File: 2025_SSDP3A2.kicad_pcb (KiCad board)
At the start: 4 copper layers, 58.4 x 28.8 mm, 62 parts, among them J1 SolderPad, J2 SolderPad, J3 SolderPad, J4 SolderPad, Q1 CSD19534Q5A, Q2 BSC0805LS, U1 LM5146RGYR

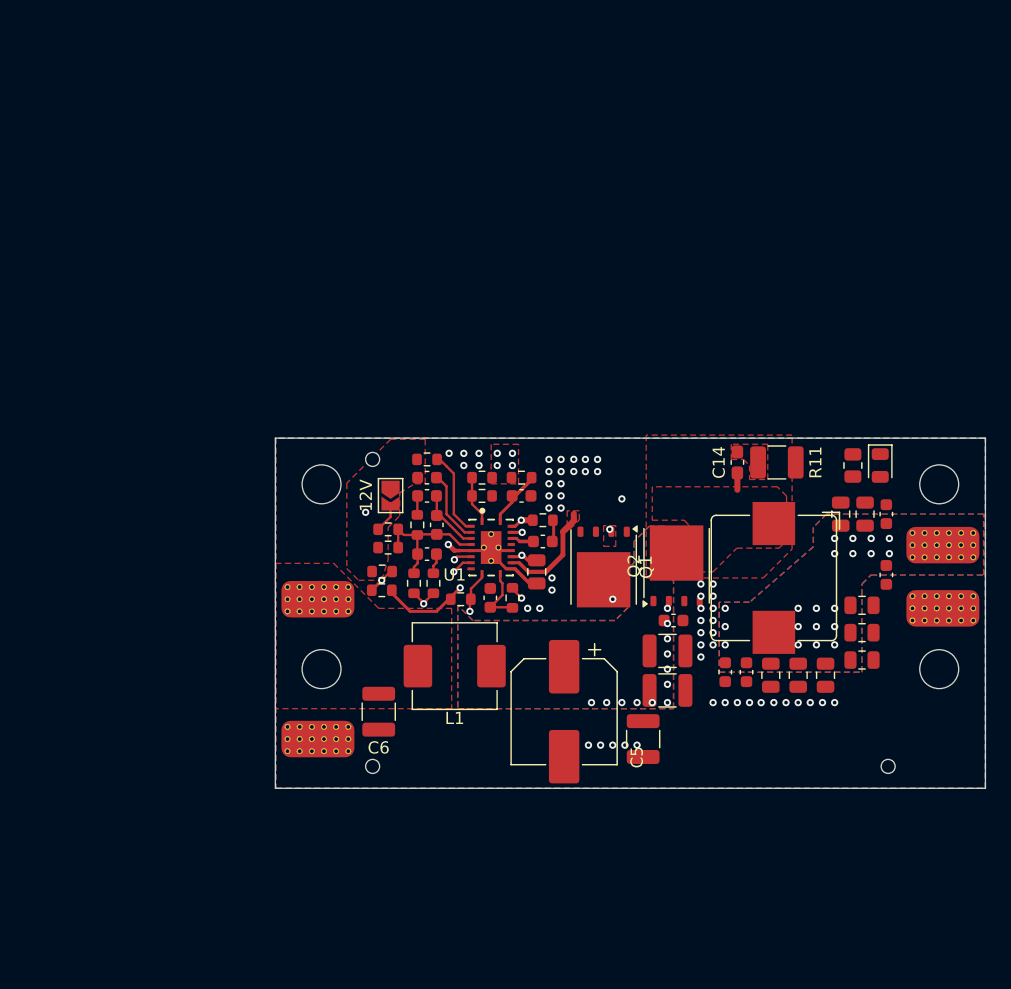
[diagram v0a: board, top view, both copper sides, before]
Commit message: Revised PCB layout
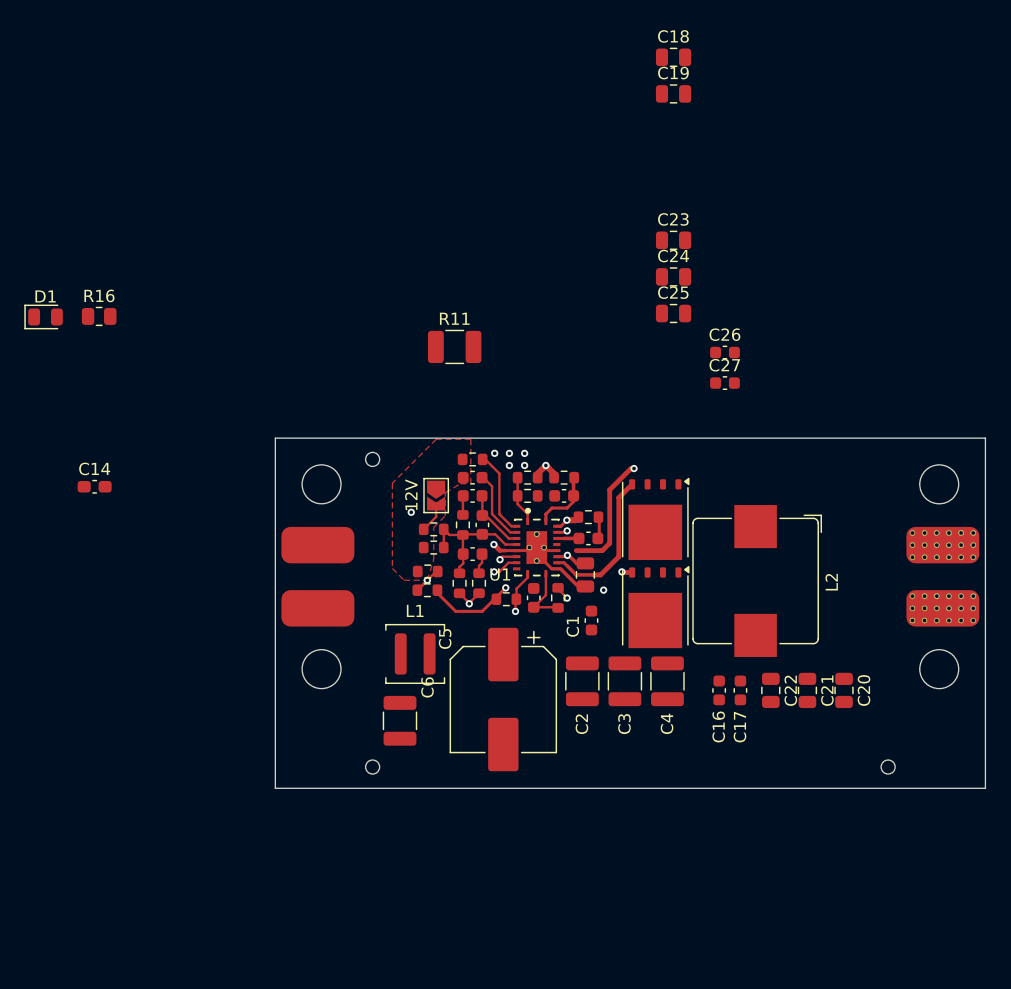
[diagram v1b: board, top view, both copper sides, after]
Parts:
- L1: footprint Inductor_SMD:L_Changjiang_FXL0630 -> Inductor_SMD:L_Coilcraft_XAL4040-XXX
- moved D1 69.7 mm to (101.1, 90.0), turned to 0 degrees
- moved R16 63.2 mm to (105.5, 90.0), turned to 0 degrees
- moved C14 52.9 mm to (105.1, 104.0), turned to 0 degrees
- moved C18 51.4 mm to (152.8, 68.7), turned to 0 degrees
- moved C19 48.9 mm to (152.8, 71.7), turned to 0 degrees
- moved C23 33.8 mm to (152.8, 83.7)
- moved R11 28.2 mm to (134.8, 92.5)
- moved C24 23.9 mm to (152.8, 86.7), turned to 0 degrees
- moved C25 22.8 mm to (152.8, 89.8), turned to 0 degrees
- moved C27 20.6 mm to (157.0, 95.5), turned to 0 degrees
- moved C26 18.8 mm to (157.0, 93.0), turned to 0 degrees
- moved J2 10.8 mm to (123.5, 114.0), turned to 90 degrees
- moved C22 8.88 mm to (160.8, 120.8), turned to -90 degrees
- moved C2 7.43 mm to (145.2, 120.0), turned to -90 degrees
- moved C1 6.75 mm to (146.0, 115.0), turned to 90 degrees
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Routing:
- net /SW: track 21.2 -> 3.47 mm, vias 5 -> 2
- net PGND: track 5.67 -> 16.2 mm, vias 51 -> 7
- net /LO: track 8.91 -> 12.5 mm, vias 2 -> 0
- net VIN: track 0.00 -> 2.56 mm, vias 16 -> 1
- net /U1_VIN: track 4.66 -> 5.29 mm
- net /HO: track 8.23 -> 7.62 mm
- net VOUT: vias 21 -> 1
- removed copper zone on F.Cu, net /HO
- removed copper zone on F.Cu, net /LO
- removed copper zone on F.Cu, net /SNUB_RC
- removed copper zone on F.Cu, net /SW
- removed copper zone on B.Cu, net PGND
- removed copper zone on F.Cu, net PGND
- removed copper zone on In1.Cu, net PGND
- removed copper zone on In2.Cu, net PGND
- removed copper zone on F.Cu, net VBAT
- removed copper zone on B.Cu, net VIN
- removed copper zone on F.Cu, net VIN
- removed copper zone on B.Cu, net VOUT
- removed copper zone on F.Cu, net VOUT

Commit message: Revised PCB layout
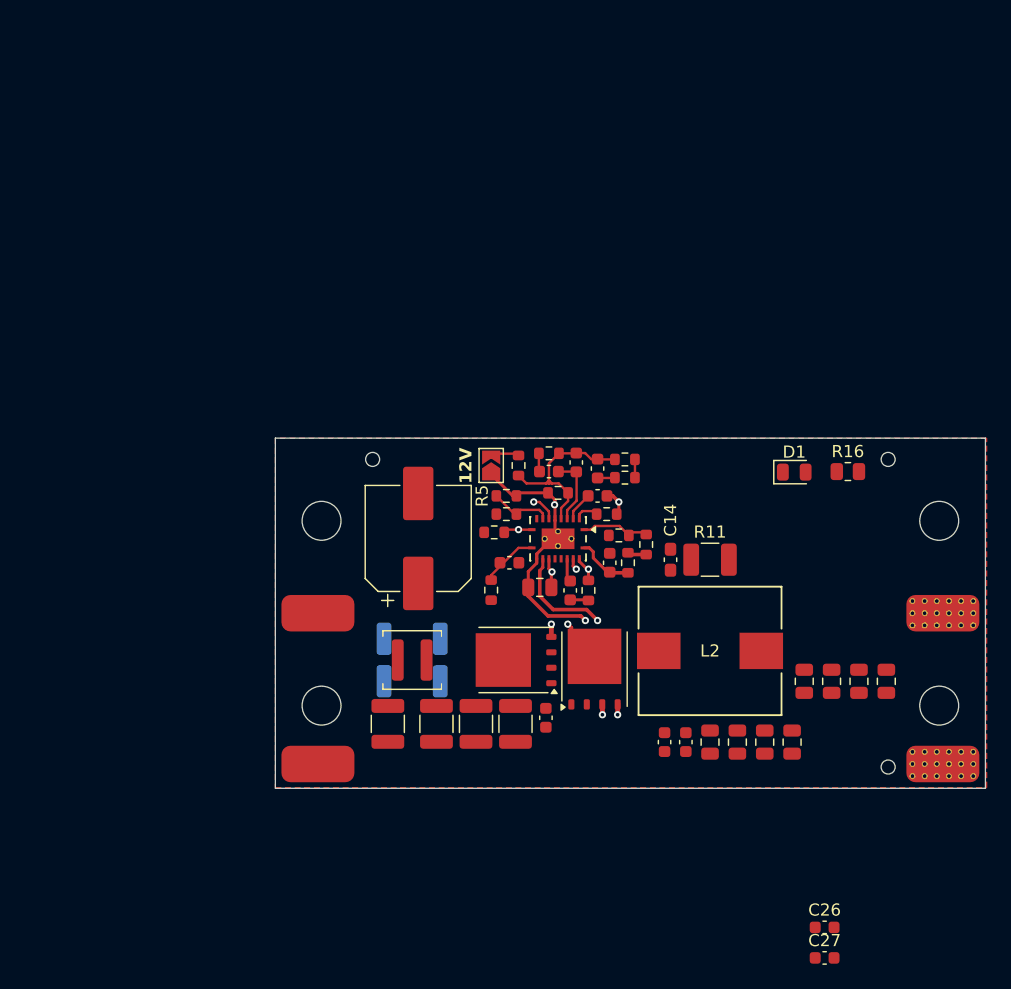
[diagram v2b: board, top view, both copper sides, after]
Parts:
- added R17: 0, Resistor_SMD:R_2010_5025Metric, B.Cu at (131.2, 116.5)
- added R18: 0, Resistor_SMD:R_2010_5025Metric, B.Cu at (131.2, 120.0)
- L2: footprint Inductor_SMD:L_Bourns_SRP1038C_10.0x10.0mm -> PA4342-472NLT:IND_PA4342_PUL-M
- Q2: value BSC0805LS -> BSC098N10NS5
- R1: value 24k -> 27k
- R3: value 9.1k -> 12k
- moved D1 62.9 mm to (162.7, 102.8)
- moved R16 62.9 mm to (167.1, 102.8)
- moved C18 56.4 mm to (155.8, 125.0), turned to -90 degrees
- moved C19 53.6 mm to (158.0, 125.0), turned to -90 degrees
- moved H5 49.4 mm to (170.4, 101.8)
- moved C26 48.0 mm to (165.2, 140.2)
- moved C27 48.0 mm to (165.2, 142.8)
- moved C14 47.7 mm to (152.5, 110.0), turned to 90 degrees
- moved C23 38.5 mm to (165.8, 120.0), turned to -90 degrees
- moved C24 36.6 mm to (168.0, 120.0), turned to -90 degrees
- moved C25 34.9 mm to (170.2, 120.0), turned to -90 degrees
- moved R11 27.3 mm to (155.8, 110.0)
- moved R14 17.0 mm to (148.8, 101.8), turned to 180 degrees
- moved C5 15.0 mm to (131.8, 108.2), turned to 90 degrees
- moved R12 14.8 mm to (148.8, 103.2), turned to 180 degrees
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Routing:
- net VCC: track 16.4 -> 2.47 mm, vias 2 -> 1
- net /SW: track 3.47 -> 10.7 mm
- net AGND: track 9.95 -> 15.5 mm
- net /LO: track 12.5 -> 17.9 mm, vias 0 -> 2
- net SYNCIN: track 10.2 -> 4.99 mm, vias 2 -> 0
- net /RT: track 7.10 -> 2.01 mm
- net PGND: track 16.2 -> 20.9 mm, vias 7 -> 2
- net /SS_TRK: track 6.39 -> 2.38 mm
- net /FB: track 11.6 -> 15.4 mm
- net /U1_EN: track 3.94 -> 5.58 mm
- net PG: track 3.48 -> 2.37 mm
- net VIN: track 2.56 -> 1.56 mm, vias 1 -> 0
- net /U1_VIN: track 5.29 -> 4.39 mm
- net VOUT: track 2.39 -> 1.50 mm, vias 1 -> 0
- net /ILIM: track 5.40 -> 4.68 mm
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- added copper zone on F.Cu, net PGND
- removed copper zone on F.Cu, net AGND
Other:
- board text added: "12V"

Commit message: Revised ILIM setting, added TVS
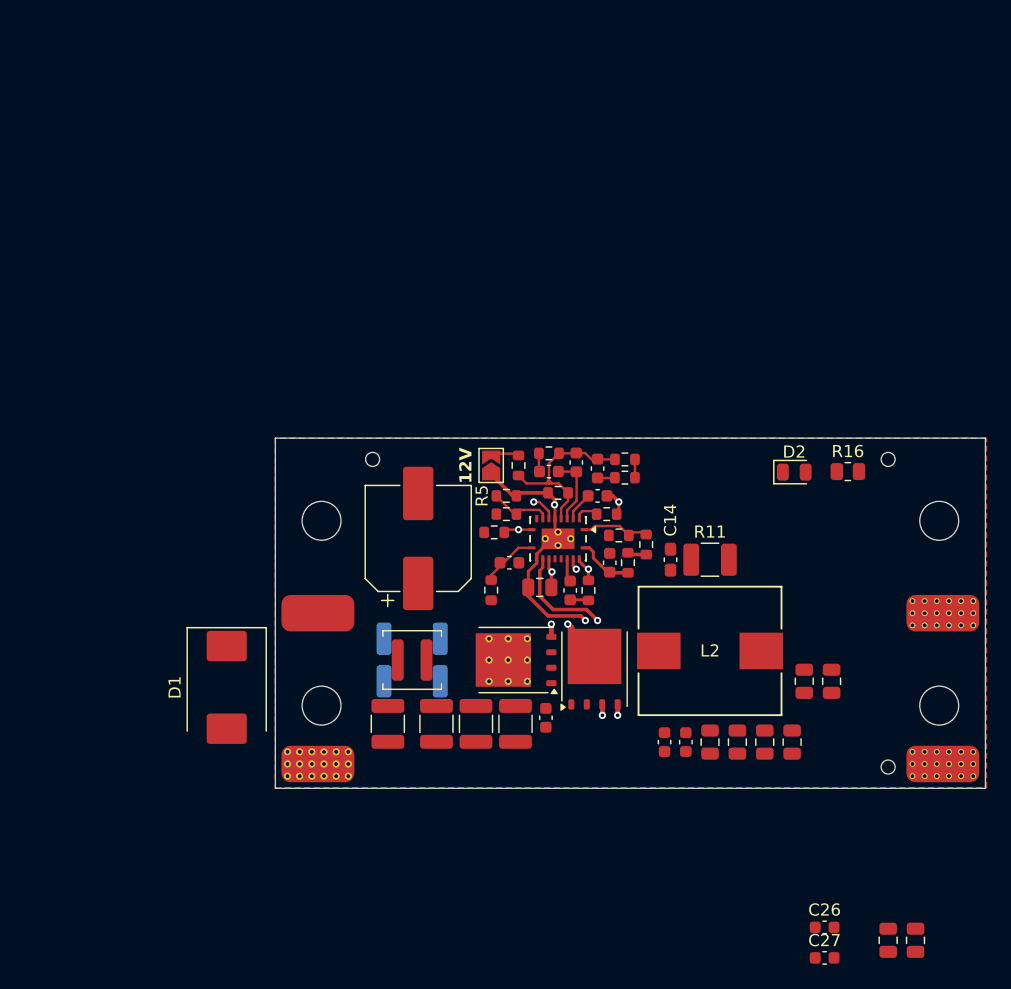
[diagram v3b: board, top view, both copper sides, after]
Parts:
- added D1: 70V, Diode_SMD:D_SMC, F.Cu at (116.0, 120.5)
- C11: value 10pF -> 22pF
- Q2: value BSC098N10NS5 -> BSC0805LS
- R8: value 470 -> 270
- moved C24 21.4 mm to (170.4, 141.3)
- moved C25 21.4 mm to (172.7, 141.3)
- renumbered D1 to D2

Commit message: Revised PCB layout, simplified EMI filter
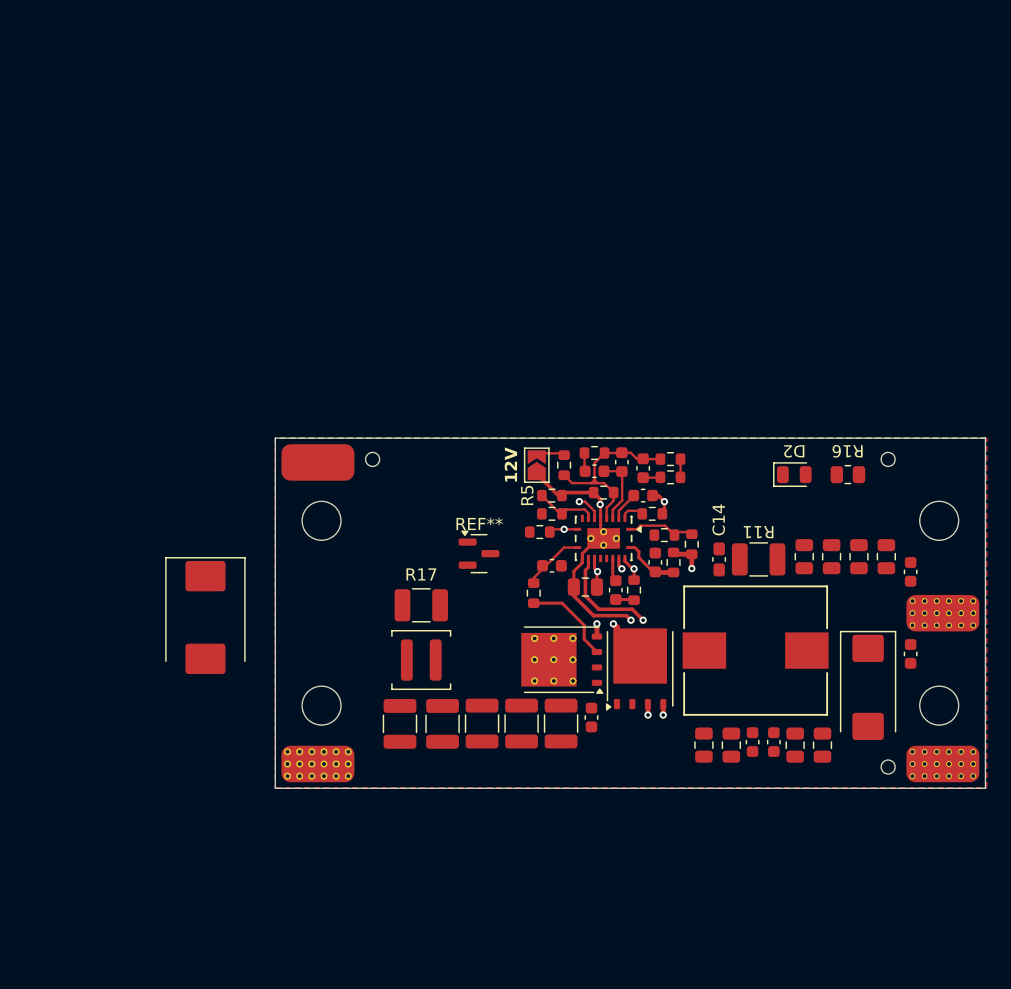
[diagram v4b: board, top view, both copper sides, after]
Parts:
- removed R18: 0, Resistor_SMD:R_2010_5025Metric
- added C28: 100uF, Capacitor_Tantalum_SMD:CP_EIA-7343-30_AVX-N_HandSolder, F.Cu at (168.8, 120.5)
- added REF**: SOT-23, Package_TO_SOT_SMD:SOT-23, F.Cu at (136.8, 109.5)
- C11: value 22pF -> 18pF
- C15: value 1nF -> 1.5nF
- C5: value 22uF -> 10uF; footprint Capacitor_SMD:CP_Elec_8x10.5 -> Capacitor_SMD:C_1210_3225Metric
- R10: value 7.5k -> 10k
- R12: value 120 -> 220
- R17: value 0 -> 10; footprint Resistor_SMD:R_2010_5025Metric -> Resistor_SMD:R_1210_3225Metric_Pad1.30x2.65mm_HandSolder; moved to F.Cu
- R8: value 270 -> 330
- moved C24 31.6 mm to (168.0, 109.8), turned to 90 degrees
- moved C25 31.6 mm to (170.2, 109.8), turned to 90 degrees
- moved C26 30.1 mm to (172.2, 111.0), turned to 90 degrees
- moved C27 26.0 mm to (172.2, 117.8), turned to -90 degrees
- moved C5 15.4 mm to (133.8, 123.5), turned to -90 degrees
- moved J1 12.4 mm to (123.5, 102.0)
- moved C22 10.2 mm to (163.5, 109.8), turned to 90 degrees
- moved C23 10.2 mm to (165.8, 109.8), turned to 90 degrees
- moved C16 7.24 mm to (159.2, 125.0)
- moved C17 7.24 mm to (161.0, 125.0)
- moved D1 6.01 mm to (114.2, 114.8)
- moved C14 4.00 mm to (156.5, 110.0)
- moved R11 4.00 mm to (159.8, 110.0)
- moved C1 3.75 mm to (146.0, 123.0)
- moved C10 3.75 mm to (148.0, 112.5)
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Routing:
- net /SW: track 10.7 -> 18.1 mm
- net VIN: track 1.56 -> 2.74 mm, vias 0 -> 1
- added copper zone on B.Cu, net PGND
- added copper zone on In1.Cu, net PGND
- added copper zone on In2.Cu, net PGND
